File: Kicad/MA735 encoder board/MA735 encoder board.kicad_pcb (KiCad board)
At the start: 2 copper layers, 5.7 x 80.4 mm, 4 parts, among them J1 FPC contacts 0.3mm, U1 MA735GGU-Z

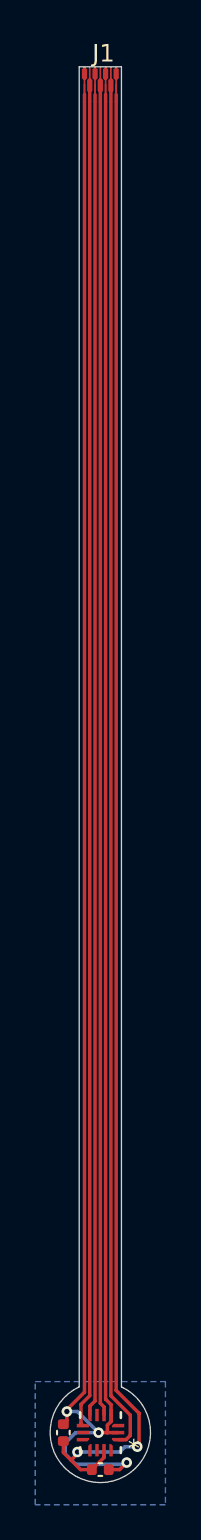
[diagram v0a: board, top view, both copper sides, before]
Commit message: Mostly finished Mainboard, adding silkscreen to magnetic encoder
I added pin headers to support my external driver board, and shrunk the whole design
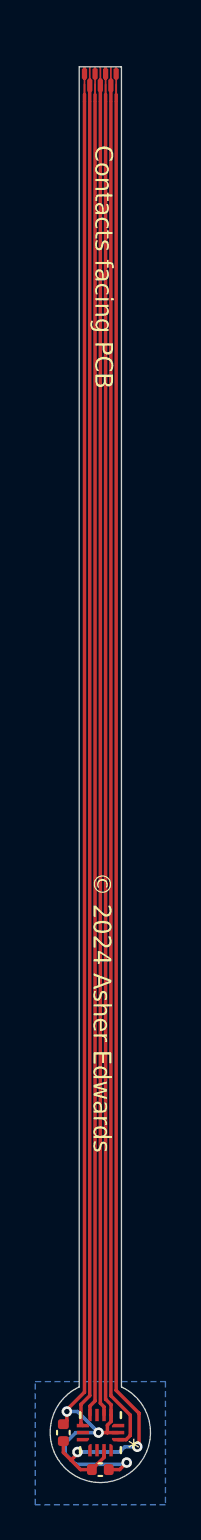
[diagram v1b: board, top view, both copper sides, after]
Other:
- board text added: "Contacts facing PCB"
- board text added: "MA735 Magnetic encoder 9-13bit, 0~60k RPM, SPI"
- board text added: "© 2024 Asher Edwards"
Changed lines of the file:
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@@
 		)
 		(property "Footprint" "MA730:UTQFN-14_MA735_MNP"
-			(at 0 0 360)
+			(at 0 0 0)
 			(layer "F.Fab")
 			(hide yes)
@@
 		)
 		(property "Datasheet" "MA735GGU-Z"
-			(at 0 0 360)
+			(at 0 0 0)
 			(layer "F.Fab")
 			(hide yes)
@@
 		)
 		(property "Description" ""
-			(at 0 0 360)
+			(at 0 0 0)
 			(layer "F.Fab")
 			(hide yes)
@@
 		)
 		(fp_text user "*"
-			(at -1.985 -0.400001 360)
+			(at -1.985 -0.400001 0)
 			(layer "F.SilkS")
 			(hide yes)
@@
 		)
 		(fp_text user "*"
-			(at -0.015 -0.4 360)
+			(at -0.015 -0.4 0)
 			(layer "F.Fab")
 			(effects
@@
 		(tags "capacitor")
 		(property "Reference" "C2"
-			(at 0 -0.1 360)
+			(at 0 -0.1 0)
 			(layer "B.SilkS")
 			(effects
@@
 		)
 		(property "Value" "0.1uF"
-			(at 0 1.16 360)
+			(at 0 1.16 0)
 			(layer "F.Fab")
 			(effects
@@
 		)
 		(fp_text user "${REFERENCE}"
-			(at 0 0 360)
+			(at 0 0 0)
 			(layer "F.Fab")
 			(effects
@@
 			(unlocked yes)
 			(layer "F.SilkS")
+			(hide yes)
 			(effects
 				(font
@@
 		(layer "User.2")
 	)
+	(gr_text "MA735 Magnetic encoder 9-13bit, 0~60k RPM, SPI"
+		(at 153.4 88.05 90)
+		(layer "B.SilkS")
+		(effects
+			(font
+				(size 1 1)
+				(thickness 0.1)
+			)
+			(justify left bottom mirror)
+		)
+	)
+	(gr_text "Contacts facing PCB"
+		(at 152.4 58.55 270)
+		(layer "F.SilkS")
+		(effects
+			(font
+				(size 1 1)
+				(thickness 0.1)
+			)
+			(justify left bottom)
+		)
+	)
+	(gr_text "© 2024 Asher Edwards"
+		(at 152.3 99.85 -90)
+		(layer "F.SilkS")
+		(effects
+			(font
+				(size 1 1)
+				(thickness 0.1)
+			)
+			(justify left bottom)
+		)
+	)
 	(gr_text "Fits connector: AYF330735 from panasonic"
